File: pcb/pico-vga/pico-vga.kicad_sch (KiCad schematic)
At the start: 27 parts, among them J1 DB15_Female_HighDensity, J2 Micro_SD_Card, J3 AudioJack3, SW1 SW_Push, U1 Raspberry_Pi_Pico, U2 74LVC2G34

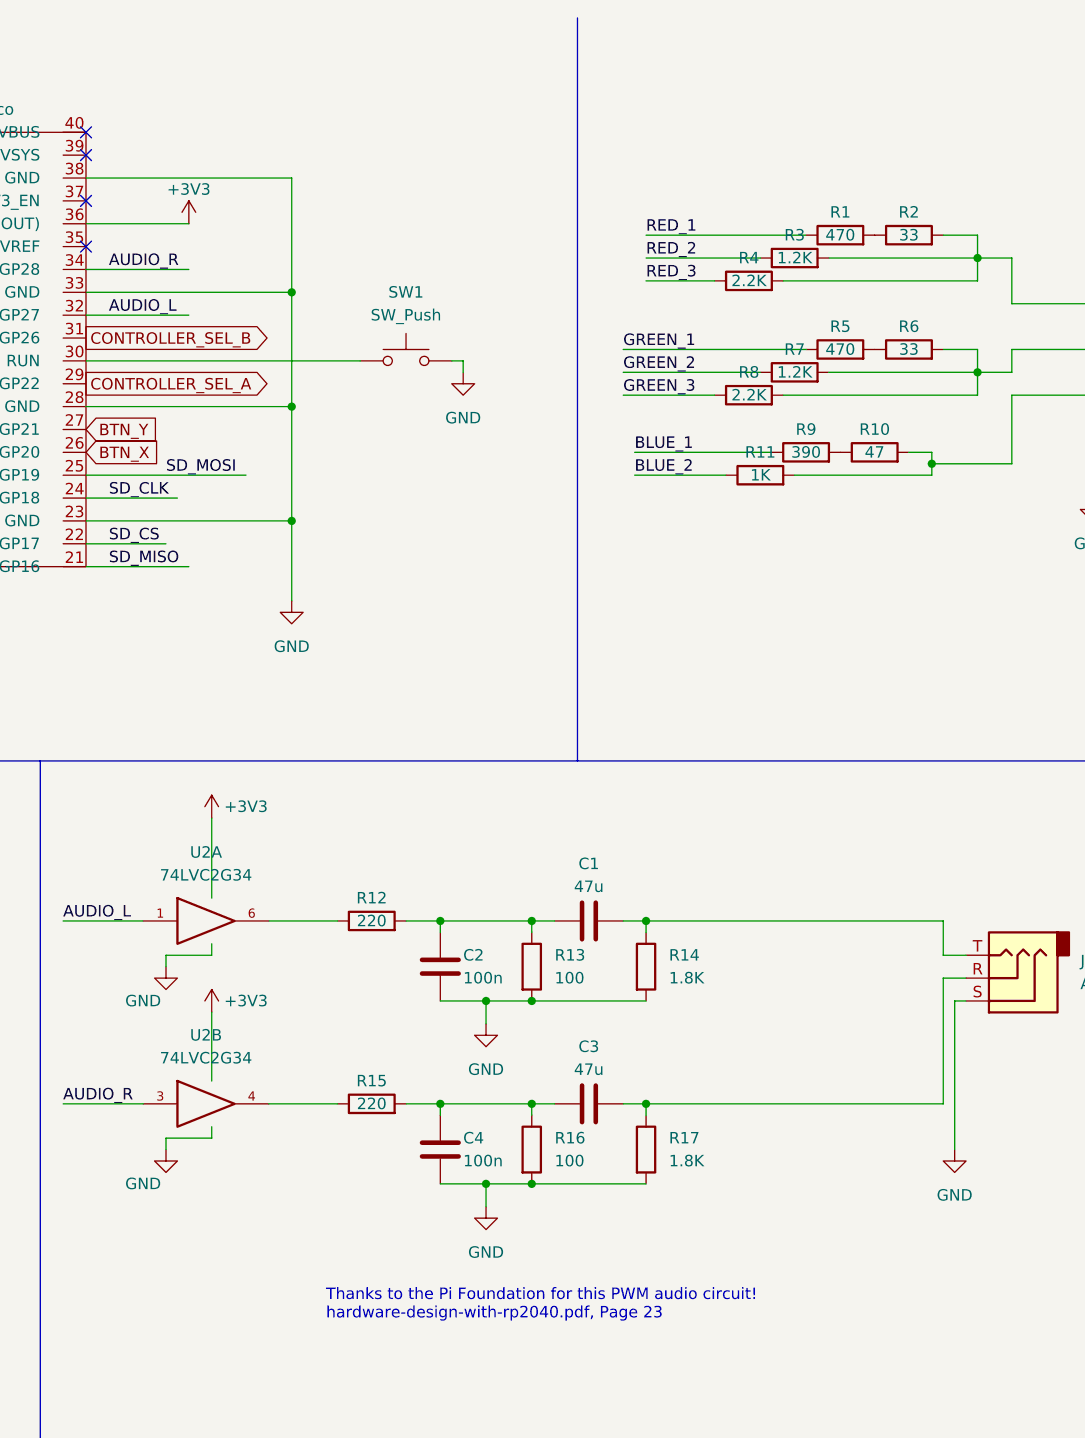
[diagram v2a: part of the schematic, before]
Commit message: pico-vga PCB DONE!!!!
It took many hours of work, and many headaches, but the board is finally done. It passes DRC, everything looks good.
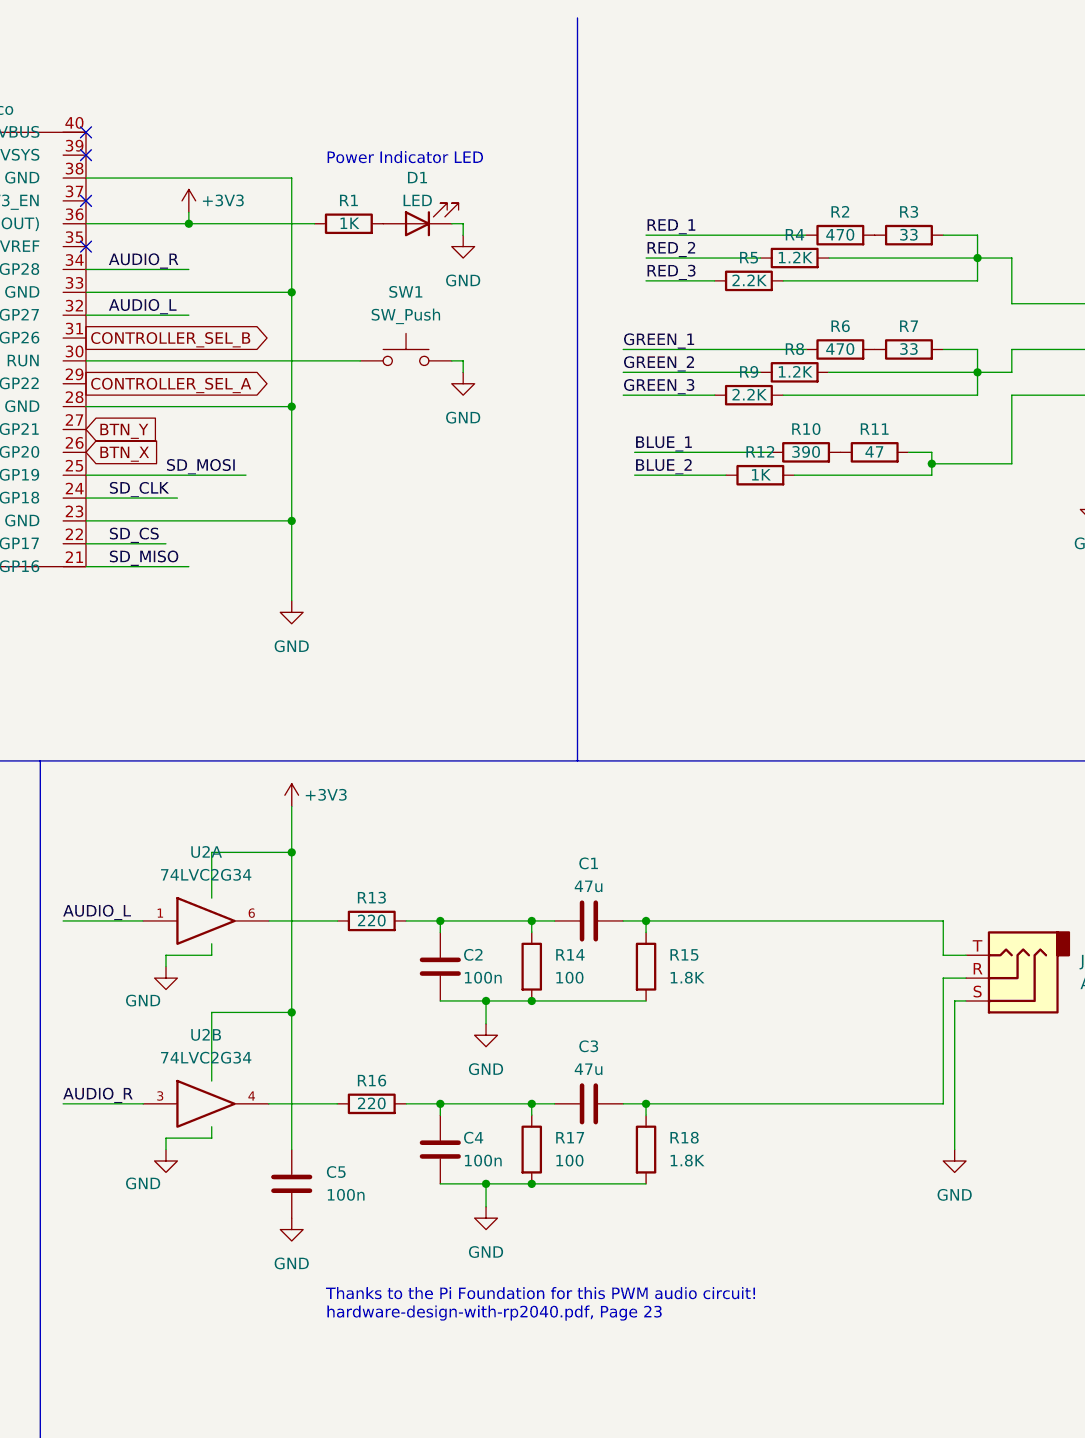
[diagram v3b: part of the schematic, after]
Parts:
- added C5: 100n, Capacitor_SMD:C_0201_0603Metric_Pad0.64x0.40mm_HandSolder, symbol Device:C
- added D1: LED, LED_SMD:LED_0805_2012Metric_Pad1.15x1.40mm_HandSolder, symbol Device:LED
- added R1: 1K, Resistor_SMD:R_0201_0603Metric_Pad0.64x0.40mm_HandSolder, symbol Device:R
- C1, C2, C3, C4: footprint (none) -> Capacitor_SMD:C_0402_1005Metric_Pad0.74x0.62mm_HandSolder
- J1: footprint (none) -> Connector_Dsub:DSUB-15-HD_Female_Horizontal_P2.29x1.98mm_EdgePinOffset8.35mm_Housed_MountingHolesOffset10.89mm
- J2: footprint (none) -> Connector_Card:microSD_HC_Hirose_DM3AT-SF-PEJM5
- J3: footprint (none) -> Connector_Audio:Jack_3.5mm_CUI_SJ1-3533NG_Horizontal
- R10: renamed from R9; footprint (none) -> Resistor_SMD:R_0603_1608Metric_Pad0.98x0.95mm_HandSolder
- R11: renamed from R10; footprint (none) -> Resistor_SMD:R_0603_1608Metric_Pad0.98x0.95mm_HandSolder
- R12: renamed from R11; footprint (none) -> Resistor_SMD:R_0603_1608Metric_Pad0.98x0.95mm_HandSolder
- R13: renamed from R12; footprint (none) -> Resistor_SMD:R_0603_1608Metric_Pad0.98x0.95mm_HandSolder
- R14: renamed from R13; footprint (none) -> Resistor_SMD:R_0603_1608Metric_Pad0.98x0.95mm_HandSolder
- R15: renamed from R14; footprint (none) -> Resistor_SMD:R_0603_1608Metric_Pad0.98x0.95mm_HandSolder
- R16: renamed from R15; footprint (none) -> Resistor_SMD:R_0603_1608Metric_Pad0.98x0.95mm_HandSolder
- R17: renamed from R16; footprint (none) -> Resistor_SMD:R_0603_1608Metric_Pad0.98x0.95mm_HandSolder
- R18: renamed from R17; footprint (none) -> Resistor_SMD:R_0603_1608Metric_Pad0.98x0.95mm_HandSolder
- R2: renamed from R1; footprint (none) -> Resistor_SMD:R_0603_1608Metric_Pad0.98x0.95mm_HandSolder
- R3: renamed from R2; footprint (none) -> Resistor_SMD:R_0603_1608Metric_Pad0.98x0.95mm_HandSolder
- R4: renamed from R3; footprint (none) -> Resistor_SMD:R_0603_1608Metric_Pad0.98x0.95mm_HandSolder
- R5: renamed from R4; footprint (none) -> Resistor_SMD:R_0603_1608Metric_Pad0.98x0.95mm_HandSolder
- R6: renamed from R5; footprint (none) -> Resistor_SMD:R_0603_1608Metric_Pad0.98x0.95mm_HandSolder
- R7: renamed from R6; footprint (none) -> Resistor_SMD:R_0603_1608Metric_Pad0.98x0.95mm_HandSolder
- R8: renamed from R7; footprint (none) -> Resistor_SMD:R_0603_1608Metric_Pad0.98x0.95mm_HandSolder
- R9: renamed from R8; footprint (none) -> Resistor_SMD:R_0603_1608Metric_Pad0.98x0.95mm_HandSolder
- SW1: footprint (none) -> Button_Switch_THT:SW_PUSH_6mm_H4.3mm
- U1: footprint (none) -> pico-vga:Raspberry_Pi_Pico
- U2: footprint (none) -> Package_SO:TSOP-6_1.65x3.05mm_P0.95mm
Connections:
- net +3V3: now also C5.1, R1.1
- net GND: now also C5.2, D1.1 (K)
- new net: D1.2 (A), R1.2
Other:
- note added: "Power Indicator LED"

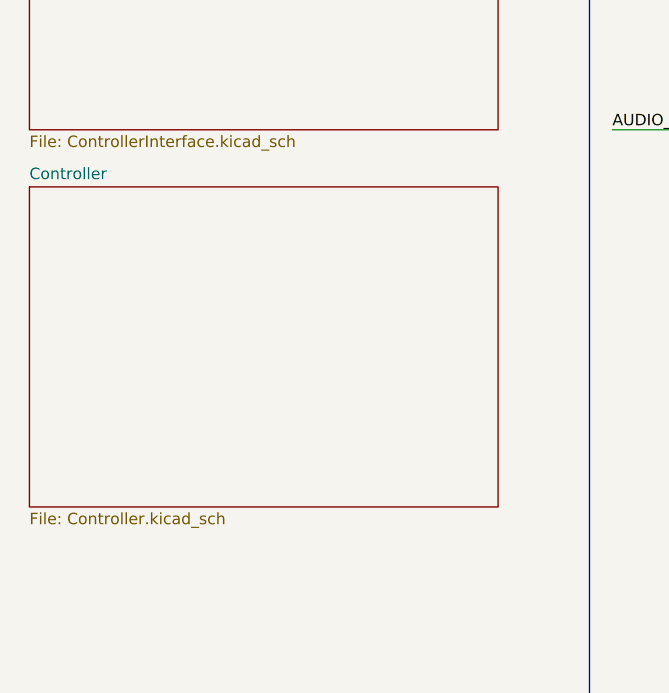
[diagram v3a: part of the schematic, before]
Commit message: Pico-VGA and Controller PCBs DONE!
Updates to pico-vga: I don't remember.... Uhhh.... I did stuff? Whatever, I like the layout, it passes DRC, it's badged, and it now has mounting holes. Updates to controller: It now exists. It also passes DRC, now has rounded corners, and has mounting holes. I'm using custom combination THT/SMD footprints for the buttons, so you can use either one depending on what you buy
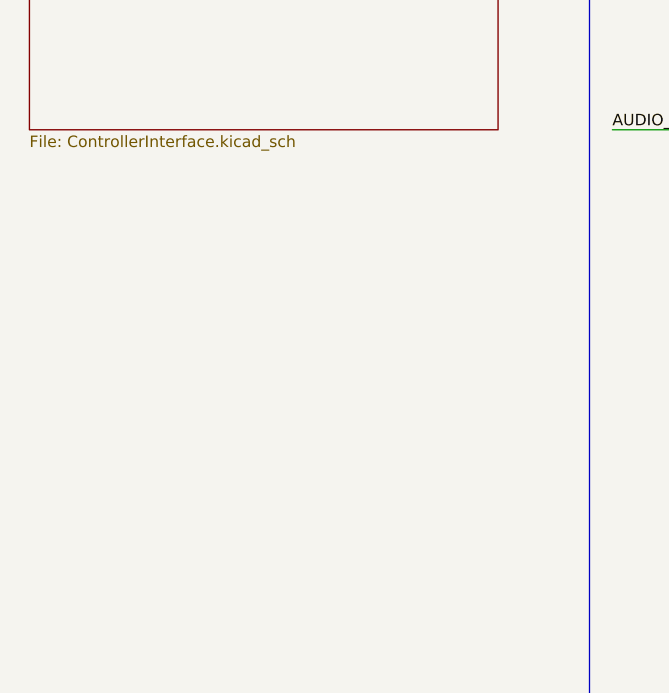
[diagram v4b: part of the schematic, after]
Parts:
- C5: footprint Capacitor_SMD:C_0201_0603Metric_Pad0.64x0.40mm_HandSolder -> Capacitor_SMD:C_0402_1005Metric_Pad0.74x0.62mm_HandSolder
- R1: footprint Resistor_SMD:R_0201_0603Metric_Pad0.64x0.40mm_HandSolder -> Resistor_SMD:R_0603_1608Metric_Pad0.98x0.95mm_HandSolder
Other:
- removed sheet Controller
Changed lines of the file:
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@@
       (effects (font (size 1.27 1.27)) (justify left))
     )
-    (property "Footprint" "Capacitor_SMD:C_0201_0603Metric_Pad0.64x0.40mm_HandSolder" (id 2) (at 105.1052 146.05 0)
+    (property "Footprint" "Capacitor_SMD:C_0402_1005Metric_Pad0.74x0.62mm_HandSolder" (id 2) (at 105.1052 146.05 0)
       (effects (font (size 1.27 1.27)) hide)
     )
@@
     (property "Reference" "R1" (id 0) (at 110.49 33.02 90))
     (property "Value" "1K" (id 1) (at 110.49 35.56 90))
-    (property "Footprint" "Resistor_SMD:R_0201_0603Metric_Pad0.64x0.40mm_HandSolder" (id 2) (at 110.49 37.338 90)
+    (property "Footprint" "Resistor_SMD:R_0603_1608Metric_Pad0.98x0.95mm_HandSolder" (id 2) (at 110.49 37.338 90)
       (effects (font (size 1.27 1.27)) hide)
     )
@@
     )
   )
-  (sheet (at 13.97 139.7) (size 52.07 35.56) (fields_autoplaced)
-    (stroke (width 0.1524) (type solid) (color 0 0 0 0))
-    (fill (color 0 0 0 0.0000))
-    (property "Sheet name" "Controller" (id 0) (at 13.97 138.9884 0)
-      (effects (font (size 1.27 1.27)) (justify left bottom))
-    )
-    (property "Sheet file" "Controller.kicad_sch" (id 1) (at 13.97 175.8446 0)
-      (effects (font (size 1.27 1.27)) (justify left top))
-    )
-  )
   (sheet_instances
     (path "/" (page "1"))
     (path "/ab8419ee-c340-452a-b70f-1668d864373f" (page "2"))
-    (path "/c8806b98-3bda-4e73-b659-fde082c72919" (page "3"))
   )
   (symbol_instances
@@
     )
     (path "/64b12867-5994-4897-9f1a-9c339521193c"
-      (reference "C5") (unit 1) (value "100n") (footprint "Capacitor_SMD:C_0201_0603Metric_Pad0.64x0.40mm_HandSolder")
+      (reference "C5") (unit 1) (value "100n") (footprint "Capacitor_SMD:C_0402_1005Metric_Pad0.74x0.62mm_HandSolder")
     )
     (path "/5e898be8-9ced-4e22-9449-60b4d0a68379"
@@
       (reference "D5") (unit 1) (value "LED") (footprint "LED_SMD:LED_0805_2012Metric_Pad1.15x1.40mm_HandSolder")
     )
-    (path "/c8806b98-3bda-4e73-b659-fde082c72919/c671c21a-a1b8-4944-a38b-cf8e78346013"
-      (reference "D6") (unit 1) (value "LED") (footprint "LED_SMD:LED_0805_2012Metric_Pad1.15x1.40mm_HandSolder")
-    )
     (path "/e46a3bb5-8a29-45cb-b6fa-4654bfb60ec8"
       (reference "J1") (unit 1) (value "DB15_Female_HighDensity") (footprint "Connector_Dsub:DSUB-15-HD_Female_Horizontal_P2.29x1.98mm_EdgePinOffset8.35mm_Housed_MountingHolesOffset10.89mm")
@@
       (reference "J7") (unit 1) (value "USB_C_Receptacle") (footprint "pico-vga:USB_C_Receptacle_Molex_2171830001")
     )
-    (path "/c8806b98-3bda-4e73-b659-fde082c72919/03b3e9d6-aa30-438c-a1d1-739c050060e1"
-      (reference "J8") (unit 1) (value "USB_C_Receptacle") (footprint "pico-vga:USB_C_Receptacle_Molex_2171830001")
-    )
     (path "/b859f1b6-6060-41ab-8a20-3be295a6de12"
-      (reference "R1") (unit 1) (value "1K") (footprint "Resistor_SMD:R_0201_0603Metric_Pad0.64x0.40mm_HandSolder")
+      (reference "R1") (unit 1) (value "1K") (footprint "Resistor_SMD:R_0603_1608Metric_Pad0.98x0.95mm_HandSolder")
     )
     (path "/bfcb33f7-85a4-4775-af32-c2f00ecf4ccc"
@@
       (reference "R26") (unit 1) (value "1M") (footprint "Resistor_SMD:R_0603_1608Metric_Pad0.98x0.95mm_HandSolder")
     )
-    (path "/c8806b98-3bda-4e73-b659-fde082c72919/729a9002-498f-4892-bd47-b1c5b6056eef"
-      (reference "R27") (unit 1) (value "1K") (footprint "Resistor_SMD:R_0603_1608Metric_Pad0.98x0.95mm_HandSolder")
-    )
     (path "/ab8419ee-c340-452a-b70f-1668d864373f/41a84cbc-dd40-4686-9e1d-7583a56adeaf"
       (reference "RN1") (unit 1) (value "10K") (footprint "Resistor_THT:R_Array_SIP9")
@@
       (reference "SW1") (unit 1) (value "SW_Push") (footprint "Button_Switch_THT:SW_PUSH_6mm_H4.3mm")
     )
-    (path "/c8806b98-3bda-4e73-b659-fde082c72919/74b6a281-a5b0-4e94-95c6-1af308130e23"
-      (reference "SW2") (unit 1) (value "SW_Push") (footprint "")
-    )
-    (path "/c8806b98-3bda-4e73-b659-fde082c72919/5f42ad98-7b22-4ca2-9af2-4a61619fbed2"
-      (reference "SW3") (unit 1) (value "SW_Push") (footprint "")
-    )
-    (path "/c8806b98-3bda-4e73-b659-fde082c72919/da4458c2-acad-4de1-b9ac-5a9d207985ca"
-      (reference "SW4") (unit 1) (value "SW_Push") (footprint "")
-    )
-    (path "/c8806b98-3bda-4e73-b659-fde082c72919/b8397096-83b3-4a60-a398-bf4b003c859a"
-      (reference "SW5") (unit 1) (value "SW_Push") (footprint "")
-    )
-    (path "/c8806b98-3bda-4e73-b659-fde082c72919/a1ec13d9-4b7b-4721-9ceb-ef2ccb1b2bbe"
-      (reference "SW6") (unit 1) (value "SW_Push") (footprint "")
-    )
-    (path "/c8806b98-3bda-4e73-b659-fde082c72919/97bbda10-5178-4e1b-b6c1-264d40bae7a4"
-      (reference "SW7") (unit 1) (value "SW_Push") (footprint "")
-    )
-    (path "/c8806b98-3bda-4e73-b659-fde082c72919/2bc11203-092a-43a9-9d06-45414714a04e"
-      (reference "SW8") (unit 1) (value "SW_Push") (footprint "")
-    )
-    (path "/c8806b98-3bda-4e73-b659-fde082c72919/d01d2b78-6ad6-492e-a23e-49cebebd9a7c"
-      (reference "SW9") (unit 1) (value "SW_Push") (footprint "")
-    )
     (path "/a5758888-1208-4297-a47a-c166319c0e7f"

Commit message: footprint fixes
some parts were not available in the footprint I picked for them, so I had to make some swaps. Also updated BOM doc
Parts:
- C1, C2, C3, C4, C5: footprint Capacitor_SMD:C_0402_1005Metric_Pad0.74x0.62mm_HandSolder -> Capacitor_SMD:C_0603_1608Metric_Pad1.08x0.95mm_HandSolder
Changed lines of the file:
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@@
       (effects (font (size 1.27 1.27)) (justify left))
     )
-    (property "Footprint" "Capacitor_SMD:C_0402_1005Metric_Pad0.74x0.62mm_HandSolder" (id 2) (at 121.6152 121.92 0)
+    (property "Footprint" "Capacitor_SMD:C_0603_1608Metric_Pad1.08x0.95mm_HandSolder" (id 2) (at 121.6152 121.92 0)
       (effects (font (size 1.27 1.27)) hide)
     )
@@
       (effects (font (size 1.27 1.27)) (justify left))
     )
-    (property "Footprint" "Capacitor_SMD:C_0402_1005Metric_Pad0.74x0.62mm_HandSolder" (id 2) (at 105.1052 146.05 0)
+    (property "Footprint" "Capacitor_SMD:C_0603_1608Metric_Pad1.08x0.95mm_HandSolder" (id 2) (at 105.1052 146.05 0)
       (effects (font (size 1.27 1.27)) hide)
     )
@@
       (effects (font (size 1.27 1.27)) (justify left))
     )
-    (property "Footprint" "Capacitor_SMD:C_0402_1005Metric_Pad0.74x0.62mm_HandSolder" (id 2) (at 121.6152 142.24 0)
+    (property "Footprint" "Capacitor_SMD:C_0603_1608Metric_Pad1.08x0.95mm_HandSolder" (id 2) (at 121.6152 142.24 0)
       (effects (font (size 1.27 1.27)) hide)
     )
@@
     (property "Reference" "C1" (id 0) (at 137.16 106.68 90))
     (property "Value" "47u" (id 1) (at 137.16 109.22 90))
-    (property "Footprint" "Capacitor_SMD:C_0402_1005Metric_Pad0.74x0.62mm_HandSolder" (id 2) (at 140.97 112.0648 0)
+    (property "Footprint" "Capacitor_SMD:C_0603_1608Metric_Pad1.08x0.95mm_HandSolder" (id 2) (at 140.97 112.0648 0)
       (effects (font (size 1.27 1.27)) hide)
     )
@@
     (property "Reference" "C3" (id 0) (at 137.16 127 90))
     (property "Value" "47u" (id 1) (at 137.16 129.54 90))
-    (property "Footprint" "Capacitor_SMD:C_0402_1005Metric_Pad0.74x0.62mm_HandSolder" (id 2) (at 140.97 132.3848 0)
+    (property "Footprint" "Capacitor_SMD:C_0603_1608Metric_Pad1.08x0.95mm_HandSolder" (id 2) (at 140.97 132.3848 0)
       (effects (font (size 1.27 1.27)) hide)
     )
@@
     )
     (path "/c77c9952-c7ee-4427-a30e-51e1c7b51b0c"
-      (reference "C1") (unit 1) (value "47u") (footprint "Capacitor_SMD:C_0402_1005Metric_Pad0.74x0.62mm_HandSolder")
+      (reference "C1") (unit 1) (value "47u") (footprint "Capacitor_SMD:C_0603_1608Metric_Pad1.08x0.95mm_HandSolder")
     )
     (path "/5eb3cabb-b195-4ef4-b998-ea6af814c3b4"
-      (reference "C2") (unit 1) (value "100n") (footprint "Capacitor_SMD:C_0402_1005Metric_Pad0.74x0.62mm_HandSolder")
+      (reference "C2") (unit 1) (value "100n") (footprint "Capacitor_SMD:C_0603_1608Metric_Pad1.08x0.95mm_HandSolder")
     )
     (path "/e8783e7d-a67a-4d0e-bc32-25a001dc8cd9"
-      (reference "C3") (unit 1) (value "47u") (footprint "Capacitor_SMD:C_0402_1005Metric_Pad0.74x0.62mm_HandSolder")
+      (reference "C3") (unit 1) (value "47u") (footprint "Capacitor_SMD:C_0603_1608Metric_Pad1.08x0.95mm_HandSolder")
     )
     (path "/8577f523-e2d7-4e57-b933-22692ca54395"
-      (reference "C4") (unit 1) (value "100n") (footprint "Capacitor_SMD:C_0402_1005Metric_Pad0.74x0.62mm_HandSolder")
+      (reference "C4") (unit 1) (value "100n") (footprint "Capacitor_SMD:C_0603_1608Metric_Pad1.08x0.95mm_HandSolder")
     )
     (path "/64b12867-5994-4897-9f1a-9c339521193c"
-      (reference "C5") (unit 1) (value "100n") (footprint "Capacitor_SMD:C_0402_1005Metric_Pad0.74x0.62mm_HandSolder")
+      (reference "C5") (unit 1) (value "100n") (footprint "Capacitor_SMD:C_0603_1608Metric_Pad1.08x0.95mm_HandSolder")
     )
     (path "/5e898be8-9ced-4e22-9449-60b4d0a68379"

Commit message: added auxiliary SPI and power headers to pcb
added a header for SPI to the board, so the board can act as a peripheral for other devices, and data/commands can be sent over SPI. also added auxiliary power connector, meant to be used when the board is in peripheral mode.
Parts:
- added J8: Conn_01x05_Male, Connector_PinHeader_2.54mm:PinHeader_1x05_P2.54mm_Horizontal, symbol Connector:Conn_01x05_Male
- added J9: Conn_01x02_Male, Connector_PinHeader_2.54mm:PinHeader_1x02_P2.54mm_Horizontal, symbol Connector:Conn_01x02_Male
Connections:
- net GND: now also J8.1 (Pin_1), J9.1 (Pin_1)
- net SD_CLK: now also J8.3 (Pin_3)
- net SD_CS: now also J8.2 (Pin_2)
- net SD_MISO: now also J8.5 (Pin_5)
- net SD_MOSI: now also J8.4 (Pin_4)
- net +5V: now reaches U1.39 (VSYS)
- net +5V: now also J9.2 (Pin_2)
- no-connect marks 11 -> 10
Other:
- note added: "Auxiliary Connection Headers"
- note added: "Can be anything 1.8-5.5VDC"
